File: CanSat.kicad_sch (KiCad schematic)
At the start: 0 parts

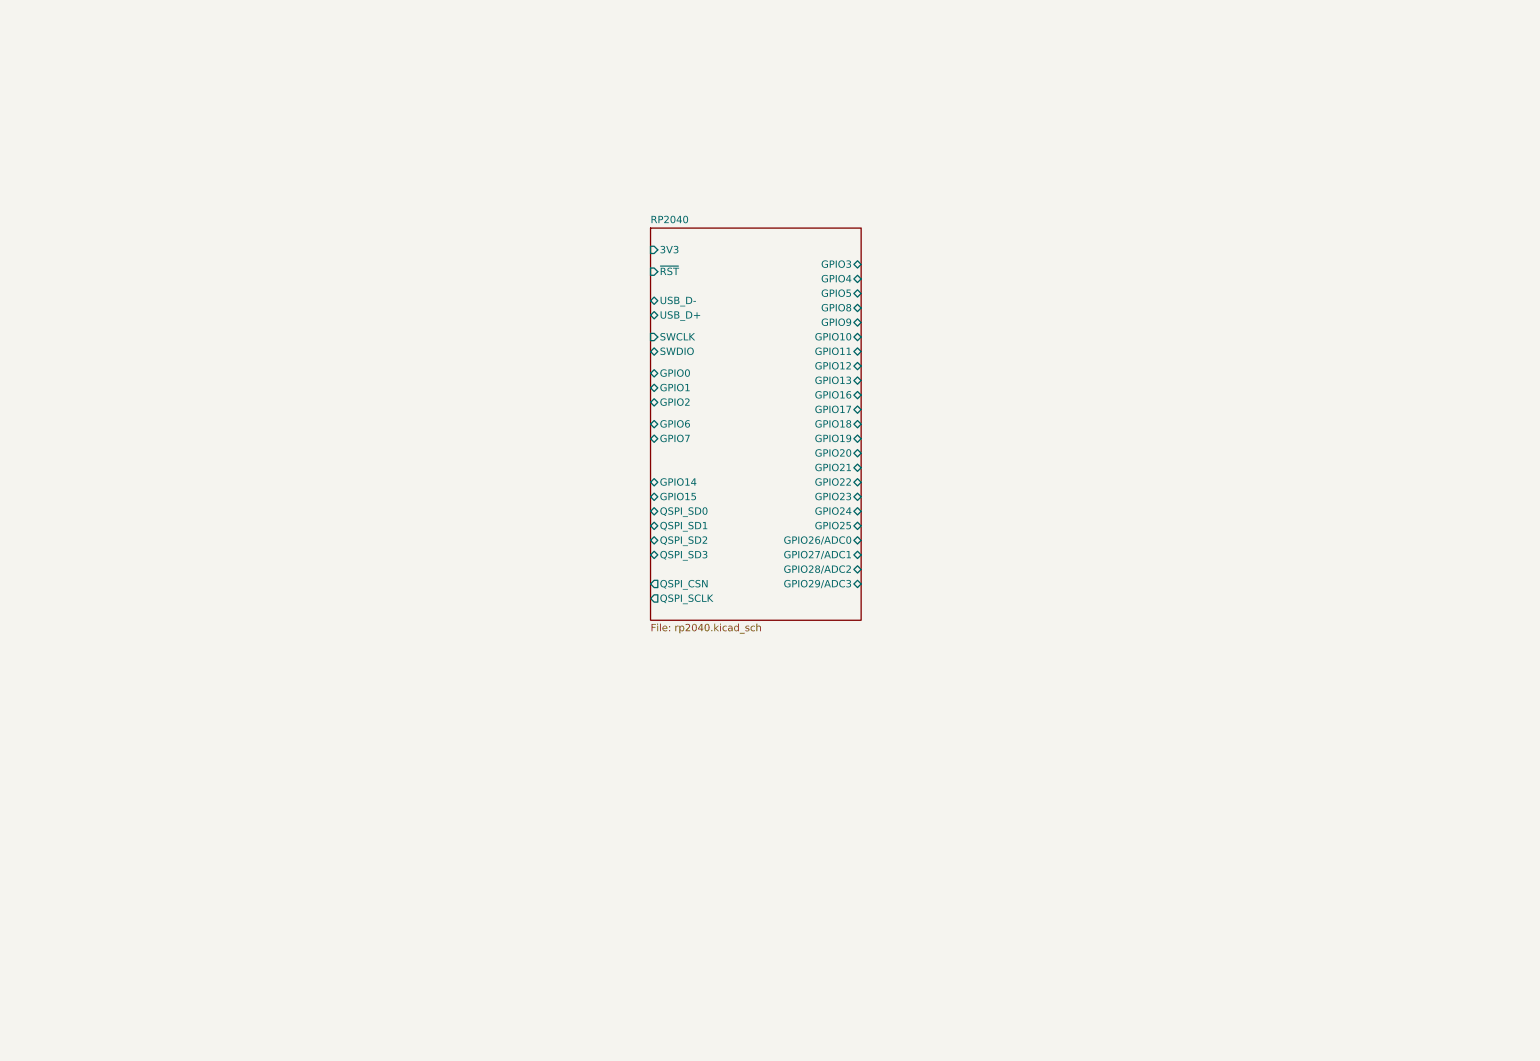
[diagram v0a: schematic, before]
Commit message: Added usb-c, buttons, memory and updated rp2040
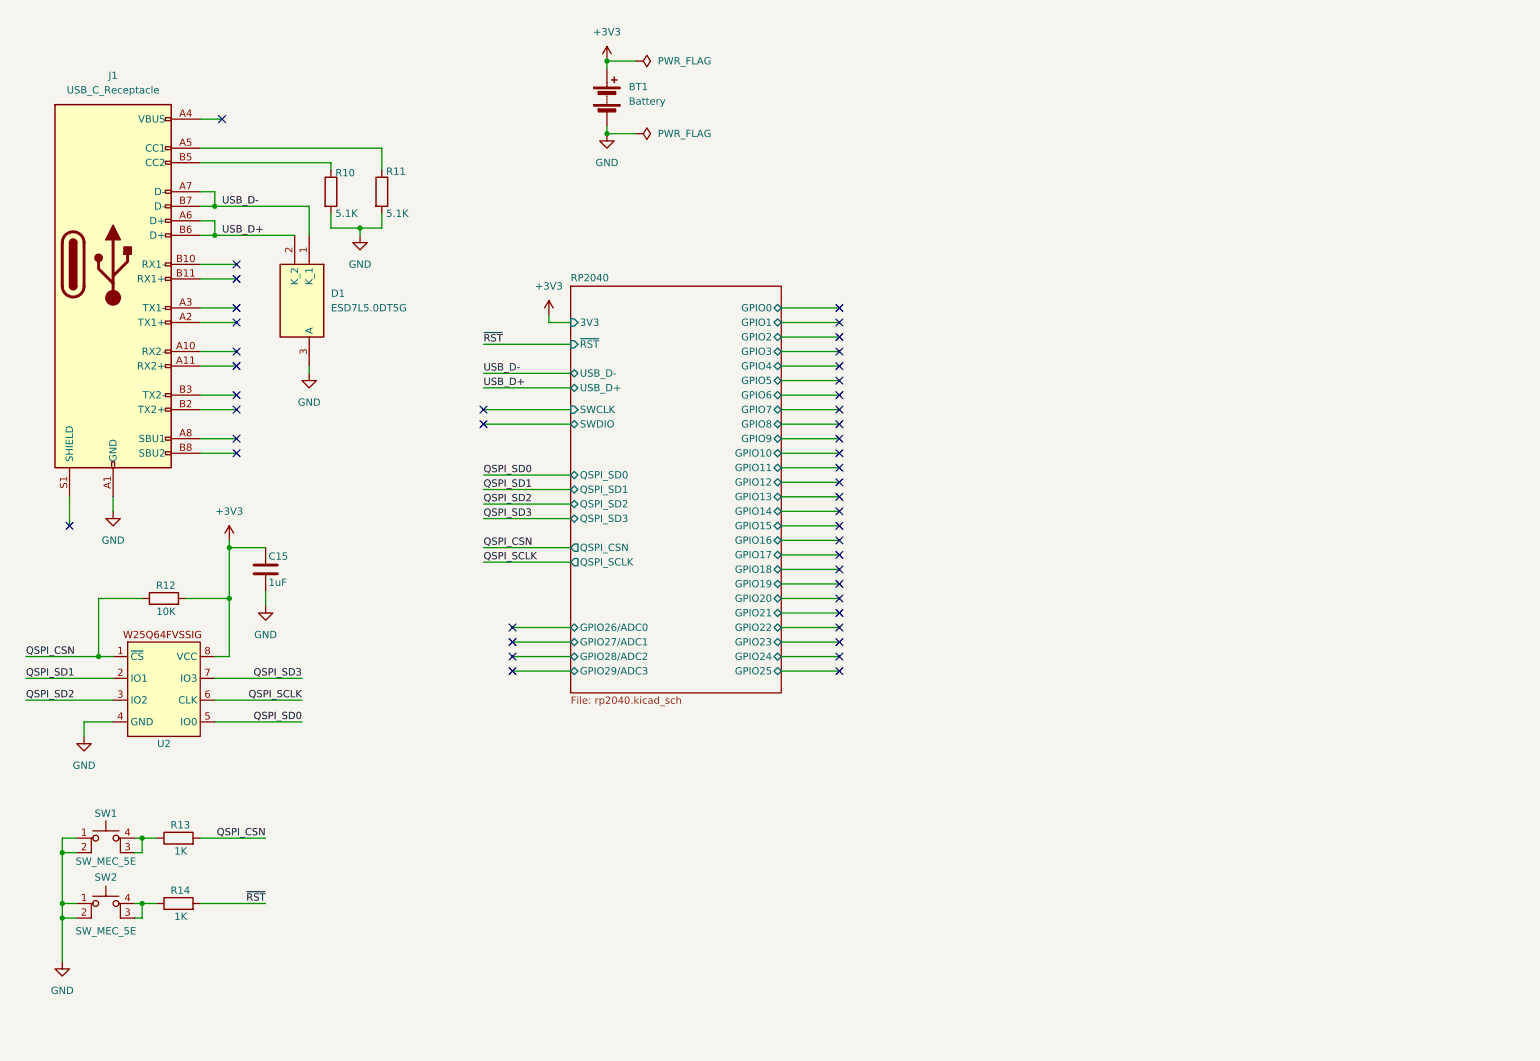
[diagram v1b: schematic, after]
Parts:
- added BT1: Battery, symbol Device:Battery
- added C15: 1uF, symbol Device:C
- added D1: ESD7L5.0DT5G, SamacSys_Parts:MMBT2907AM3T5G, symbol SamacSys_Parts:ESD7L5.0DT5G
- added J1: USB_C_Receptacle, symbol Connector:USB_C_Receptacle
- added R10, R11: 5.1K, Resistor_THT:R_Axial_DIN0207_L6.3mm_D2.5mm_P7.62mm_Horizontal, symbol Device:R
- added R12: 10K, Resistor_THT:R_Axial_DIN0207_L6.3mm_D2.5mm_P7.62mm_Horizontal, symbol Device:R
- added R13, R14: 1K, Resistor_THT:R_Axial_DIN0207_L6.3mm_D2.5mm_P7.62mm_Horizontal, symbol Device:R
- added SW1, SW2: SW_MEC_5E, symbol Switch:SW_MEC_5E
- added U2: ~, memory:W25Q64FVSSIG, symbol memory:W25Q64FVSSIG
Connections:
- new net: R13.1, SW1.3 (K), SW1.4 (A)
- new net: R14.1, SW2.3 (K), SW2.4 (A)
- new net: J1.A4 (VBUS), J1.A9 (VBUS), J1.B4 (VBUS), J1.B9 (VBUS)
- new net: J1.A5 (CC1), R11.1
- new net: J1.B5 (CC2), R10.1
- new net +3V3: BT1.1 (+), C15.1, R12.2, U2.8 (VCC)
- new net GND: BT1.2 (-), C15.2, D1.3 (A), J1.A1 (GND), J1.A12 (GND), J1.B1 (GND), J1.B12 (GND), R10.2, R11.2, SW1.1, SW1.2, SW2.1, SW2.2, U2.4 (GND)
- new net QSPI_CSN: R12.1, R13.2, U2.1 (~{CS})
- new net QSPI_SCLK: U2.6 (CLK)
- new net QSPI_SD0: U2.5 (DI)
- new net QSPI_SD1: U2.2 (DO)
- new net QSPI_SD2: U2.3 (~{WP})
- new net QSPI_SD3: U2.7 (~{HOLD})
- new net USB_D+: D1.2 (K_2), J1.A6 (D+), J1.B6 (D+)
- new net USB_D-: D1.1 (K_1), J1.A7 (D-), J1.B7 (D-)
- new net ~{RST}: R14.2
- no-connect marks 0 -> 44

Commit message: Update schematic symbols and add new components
Switched RP2040 for RP2350A.
Added LoRa and acceloremeter + gyroscope module.
Added labels.
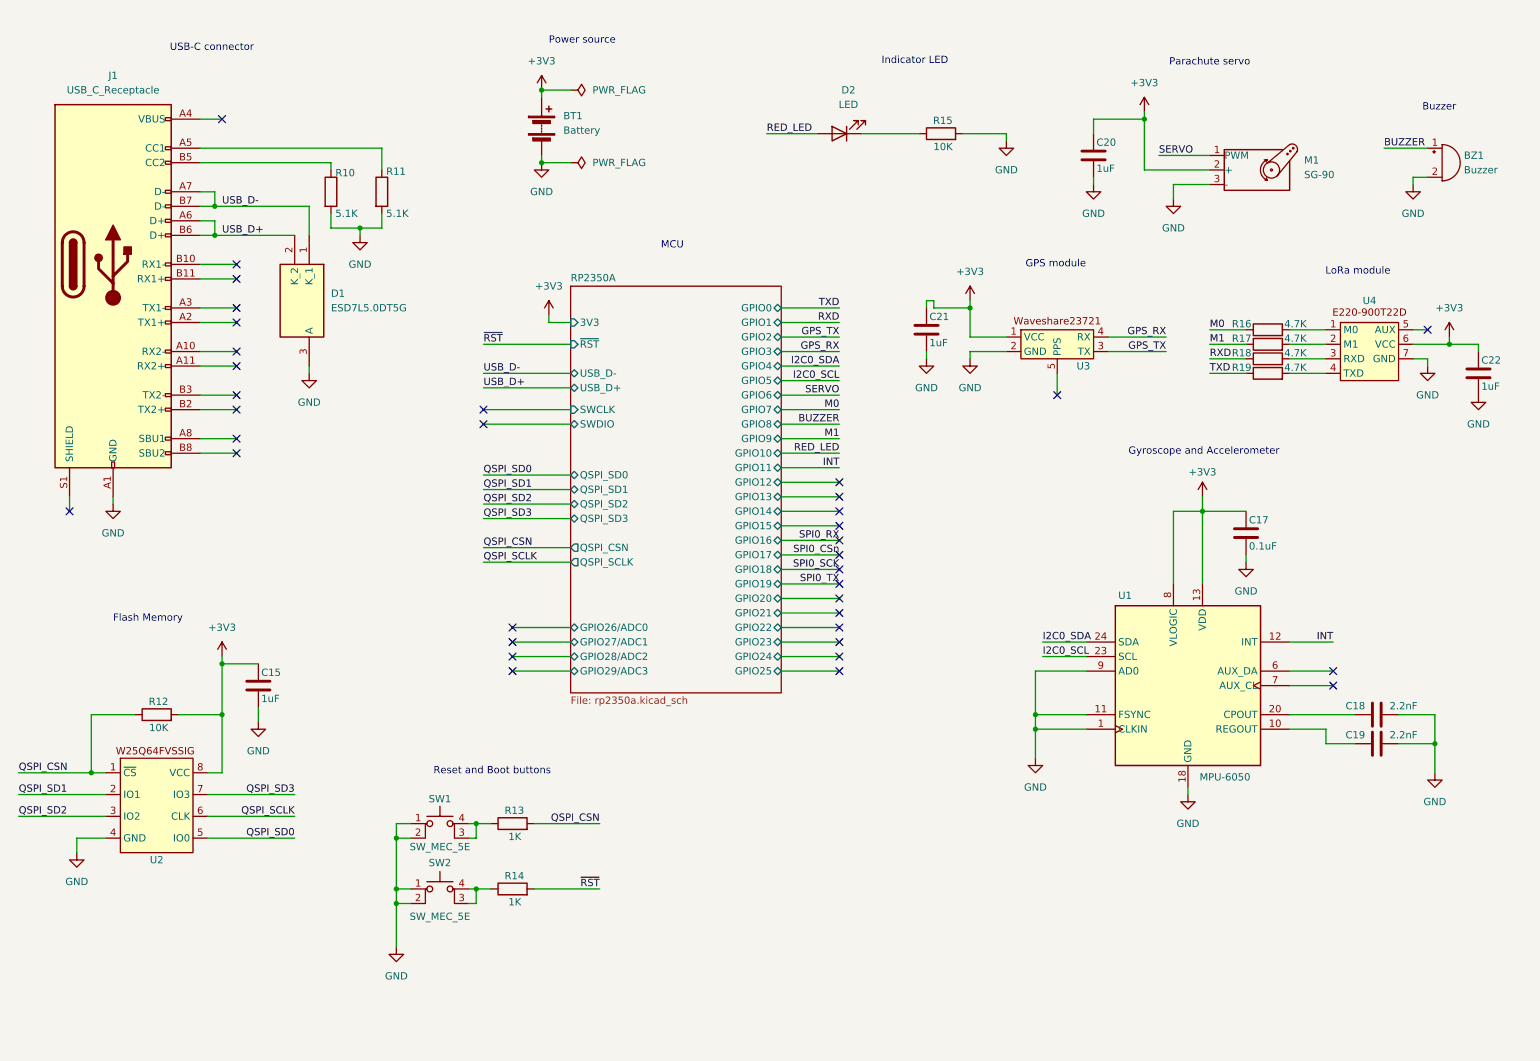
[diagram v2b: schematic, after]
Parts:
- added BZ1: Buzzer, symbol Device:Buzzer
- added C17: 0.1uF, symbol Device:C
- added C18, C19: 2.2nF, symbol Device:C
- added C20, C21, C22: 1uF, symbol Device:C
- added D2: LED, symbol Device:LED
- added M1: SG-90, symbol Motor:Motor_Servo
- added R15: 10K, Resistor_THT:R_Axial_DIN0207_L6.3mm_D2.5mm_P7.62mm_Horizontal, symbol Device:R
- added R16, R17, R18, R19: 4.7K, symbol Device:R
- added U1: MPU-6050, Sensor_Motion:InvenSense_QFN-24_4x4mm_P0.5mm, symbol Sensor_Motion:MPU-6050
- added U3: ~, symbol Waveshare:Waveshare_23721
- added U4: ~, symbol LoRa:E220-900T22D
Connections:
- net +3V3: now also C17.1, C20.1, C21.1, C22.1, M1.2 (+), U1.13 (VDD), U1.8 (VLOGIC), U3.1 (VCC), U4.6 (VCC)
- net GND: now also BZ1.2 (-), C17.2, C18.2, C19.2, C20.2, C21.2, C22.2, M1.3 (-), R15.2, U1.1 (CLKIN), U1.11 (FSYNC), U1.18 (GND), U1.9 (AD0), U3.2 (GND), U4.7 (GND)
- new net: R18.2, U4.3 (RXD)
- new net: D2.1 (K), R15.1
- new net: R17.2, U4.2 (M1)
- new net: C19.1, U1.10 (REGOUT)
- new net: C18.1, U1.20 (CPOUT)
- new net: R16.2, U4.1 (M0)
- new net: R19.2, U4.4 (TXD)
- new net BUZZER: BZ1.1 (+)
- new net GPS_RX: U3.4 (RX)
- new net GPS_TX: U3.3 (TX)
- new net I2C0_SCL: U1.23 (SCL)
- new net I2C0_SDA: U1.24 (SDA)
- new net INT: U1.12 (INT)
- new net M0: R16.1
- new net M1: R17.1
- new net RED_LED: D2.2 (A)
- new net RXD: R18.1
- new net SERVO: M1.1 (PWM)
- new net TXD: R19.1
- no-connect marks 44 -> 36
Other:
- sheet RP2040 renamed RP2350A
- sheet RP2350A: file rp2040.kicad_sch -> rp2350a.kicad_sch
- note added: "Buzzer"
- note added: "Flash Memory"
- note added: "GPS module"
- note added: "Gyroscope and Accelerometer"
- note added: "Indicator LED"
- note added: "LoRa module"
- note added: "MCU"
- note added: "Parachute servo"
- note added: "Power source"
- note added: "Reset and Boot buttons"
- note added: "USB-C connector"
- moved on the sheet: BT1, C15, R12, R13, R14, SW1, SW2, U2

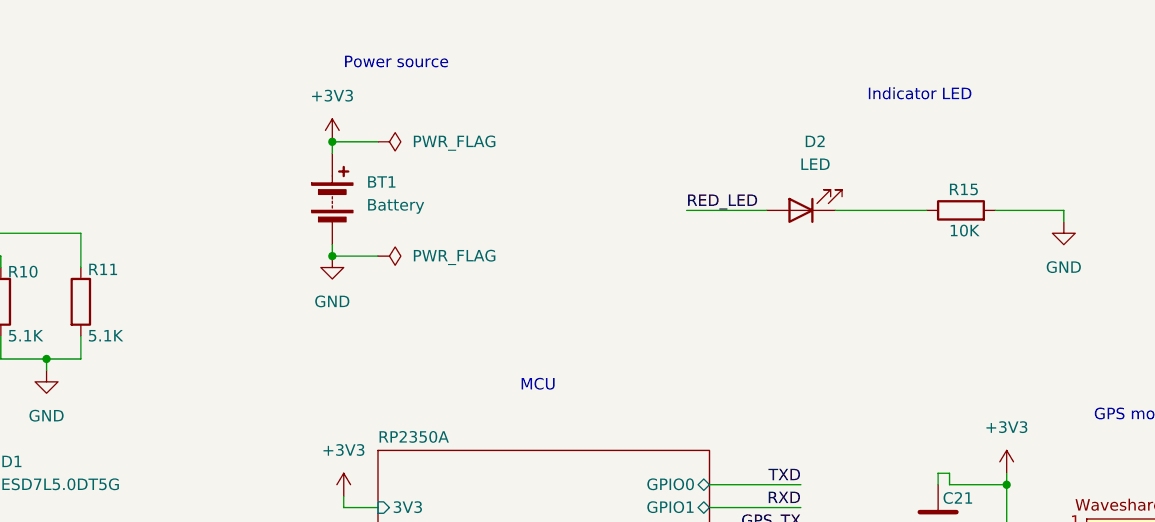
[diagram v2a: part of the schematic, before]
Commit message: add linear regulator
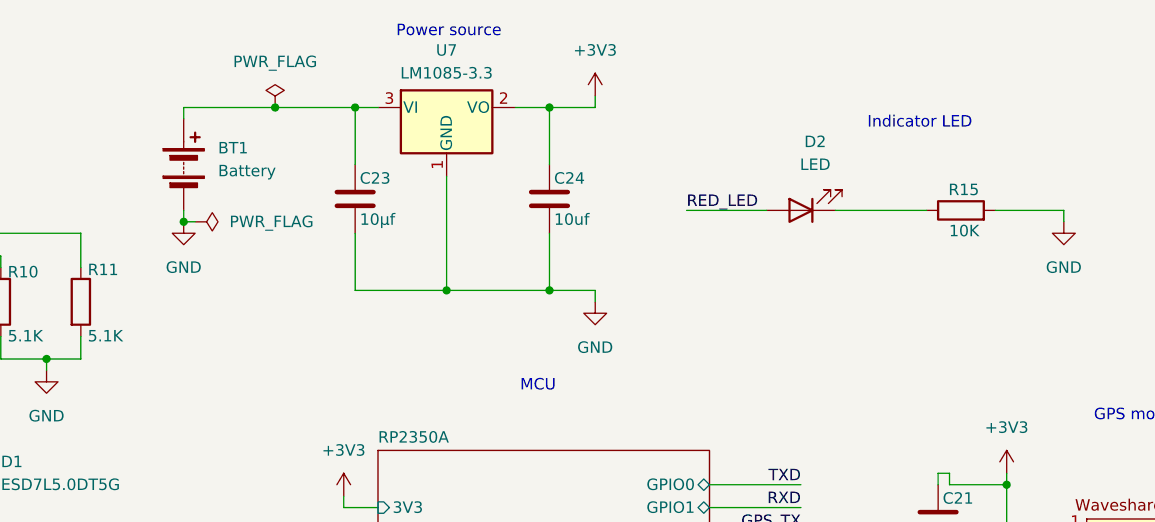
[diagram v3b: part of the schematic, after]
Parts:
- added C23: 10µf, symbol Device:C
- added C24: 10uf, symbol Device:C
- added U7: LM1085-3.3, symbol Regulator_Linear:LM1085-3.3
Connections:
- net +3V3: now also C24.1, U7.2 (VO); no longer BT1.1 (+)
- net GND: now also C23.2, C24.2, U7.1 (GND)
- new net: BT1.1 (+), C23.1, U7.3 (VI)
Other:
- moved on the sheet: BT1

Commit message: Add 5V power source
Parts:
- added BT2: Battery, symbol Device:Battery
- added C25: 10µf, symbol Device:C
- added C26: 10uf, symbol Device:C
- added U6: LM1085-5.0, symbol Regulator_Linear:LM1085-5.0
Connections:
- net +3V3: no longer C20.1, M1.2 (+)
- net GND: now also BT2.2 (-), C25.2, C26.2, U6.1 (GND)
- new net: BT2.1 (+), C25.1, U6.3 (VI)
- new net +5V: C20.1, C26.1, M1.2 (+), U6.2 (VO)
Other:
- note added: "Power source 3V3"
- note added: "Power source 5V"
- note removed: "Power source"
- moved on the sheet: C15, C17, C18, C19, D2, R12, R13, R14, R15, SW1, SW2, U1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

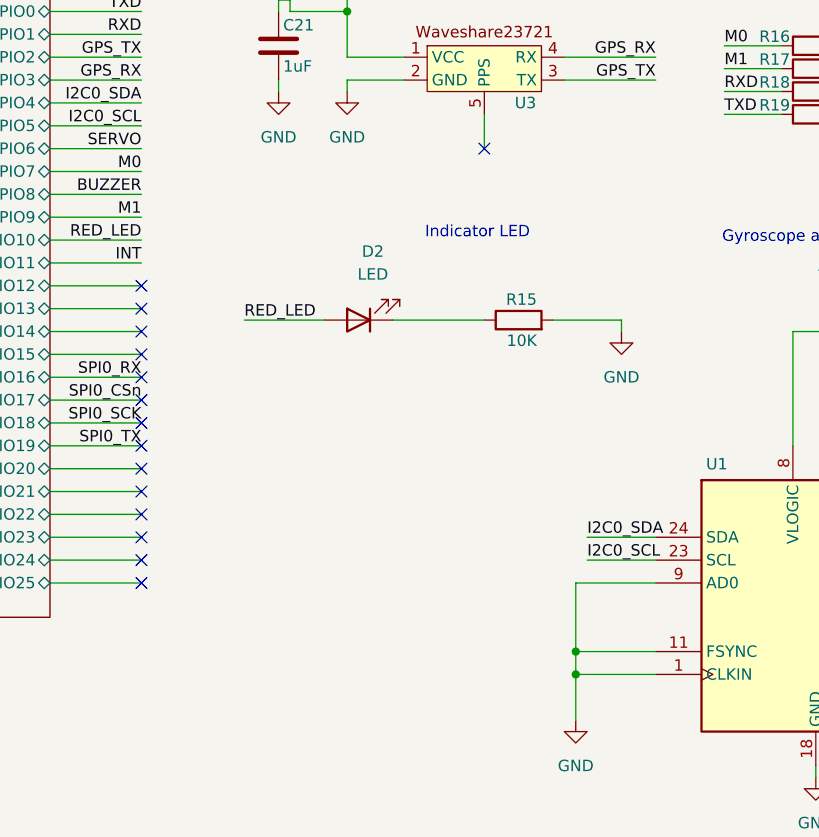
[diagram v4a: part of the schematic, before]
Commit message: Add BMP280
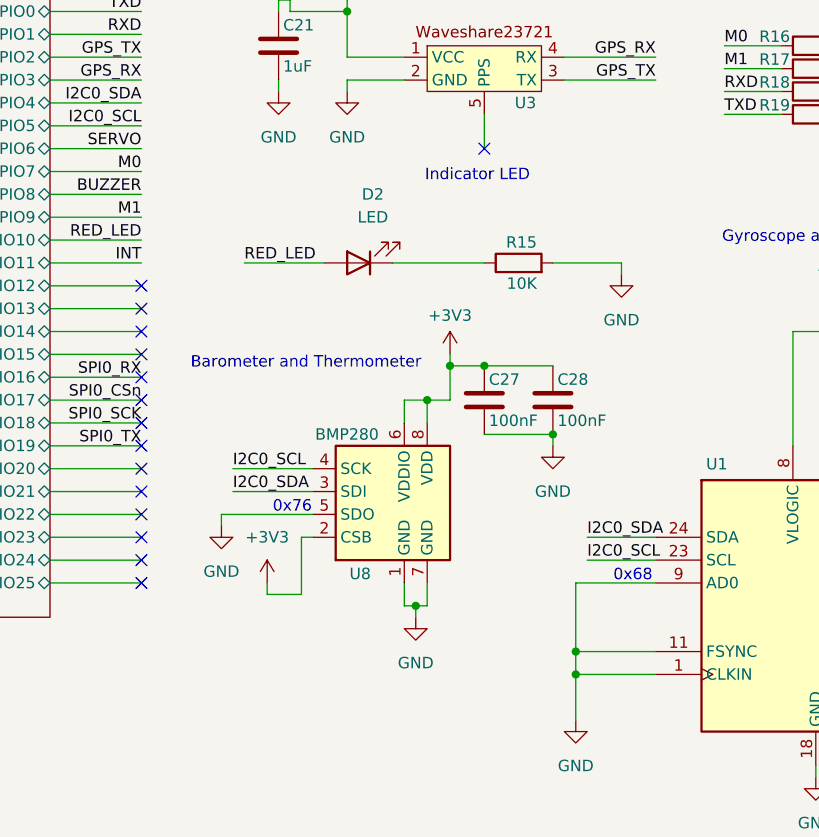
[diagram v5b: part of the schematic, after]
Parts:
- added C27, C28: 100nF, symbol Device:C
- added U8: BMP280, Package_LGA:Bosch_LGA-8_2x2.5mm_P0.65mm_ClockwisePinNumbering, symbol Sensor_Pressure:BMP280
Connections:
- net +3V3: now also C27.1, C28.1, U8.2 (CSB), U8.6 (VDDIO), U8.8 (VDD)
- net GND: now also C27.2, C28.2, U8.1 (GND), U8.5 (SDO)
- net I2C0_SCL: now also U8.4 (SCK)
- net I2C0_SDA: now also U8.3 (SDI)
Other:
- note added: "0x68"
- note added: "0x76"
- note added: "Barometer and Thermometer"
- moved on the sheet: D2, R15

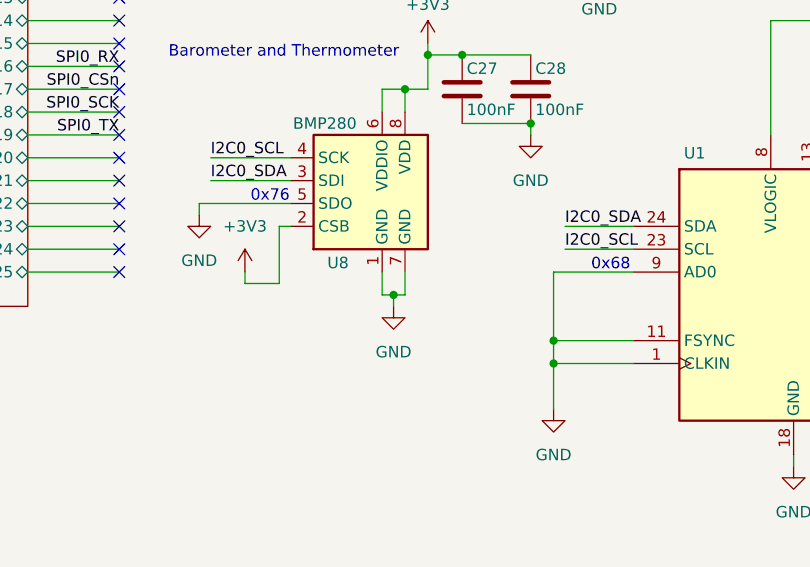
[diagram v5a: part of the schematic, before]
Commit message: Bug fix
unconnected wire
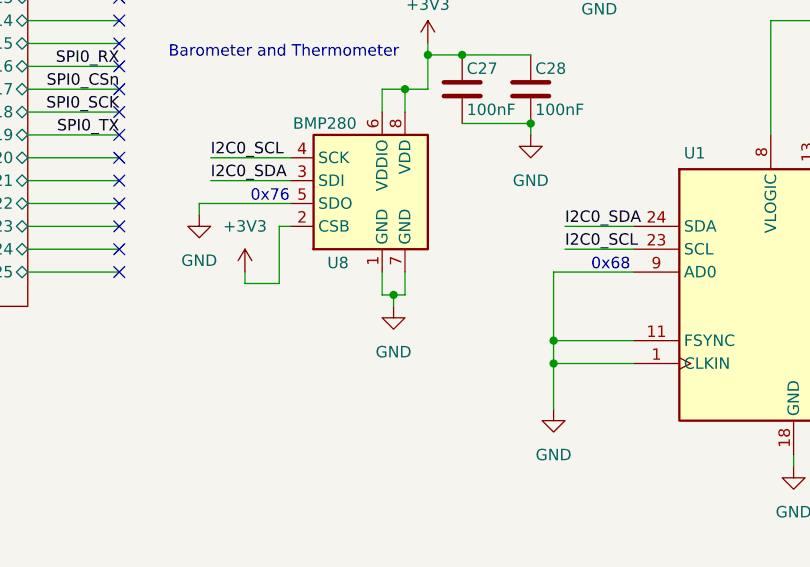
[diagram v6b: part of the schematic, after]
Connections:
- net GND: now also U8.7 (GND)
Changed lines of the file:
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@@
+	(wire
+		(pts
+			(xy 195.58 129.54) (xy 195.58 132.08)
+		)
+		(stroke
+			(width 0)
+			(type default)
+		)
+	)
 	(wire
 		(pts
@@
 		)
 		(stroke
-			(width 0)
-			(type default)
-		)
-	)
-	(wire
-		(pts
-			(xy 195.58 129.6118) (xy 195.58 132.08)
-		)
-		(stroke
